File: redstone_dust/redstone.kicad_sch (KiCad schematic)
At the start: 61 parts, among them J1 1x4_Pogo, J2 1x4_Pogo, J3 1x4_Pogo, J4 1x4_Pogo, J5 1x4_Pogo, J6 1x4_Pogo, J7 1x4_Pogo, J8 1x4_Pogo, J9 2.54mm_ProgrammingPin, Q1 BC108, Q2 BC108, Q3 BC108, Q4 BC108, SW1 SW_Push_Open, U1 RP2040, U2 RBT05W24S05, U3 TPS62162DSG, U5 W25Q16JVSS

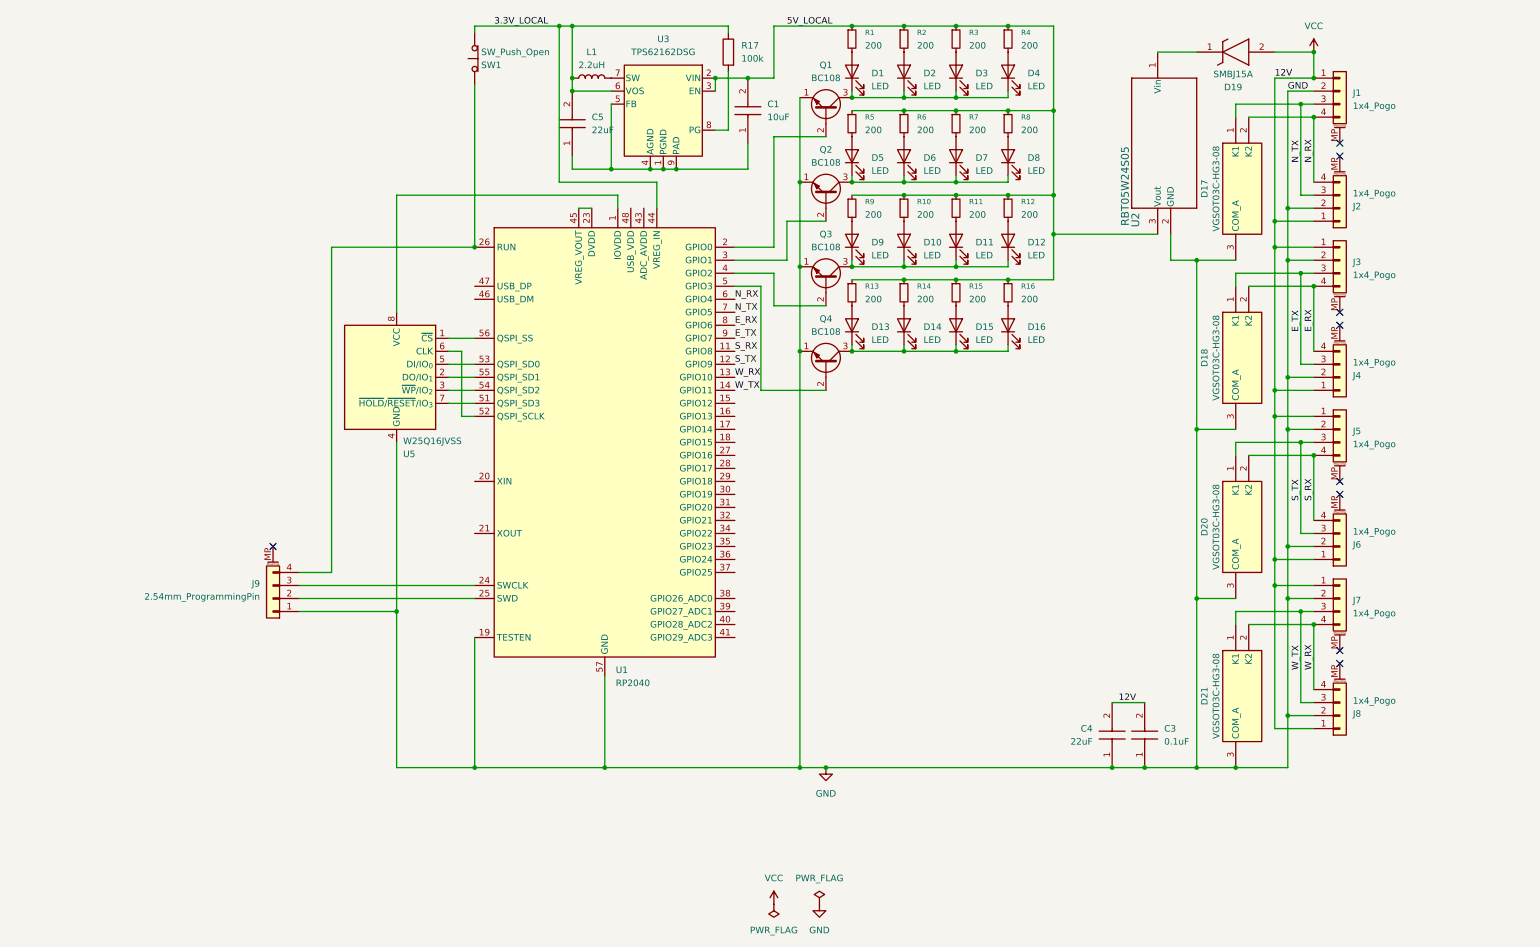
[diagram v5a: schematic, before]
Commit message: add no connect flags to unconnected pins
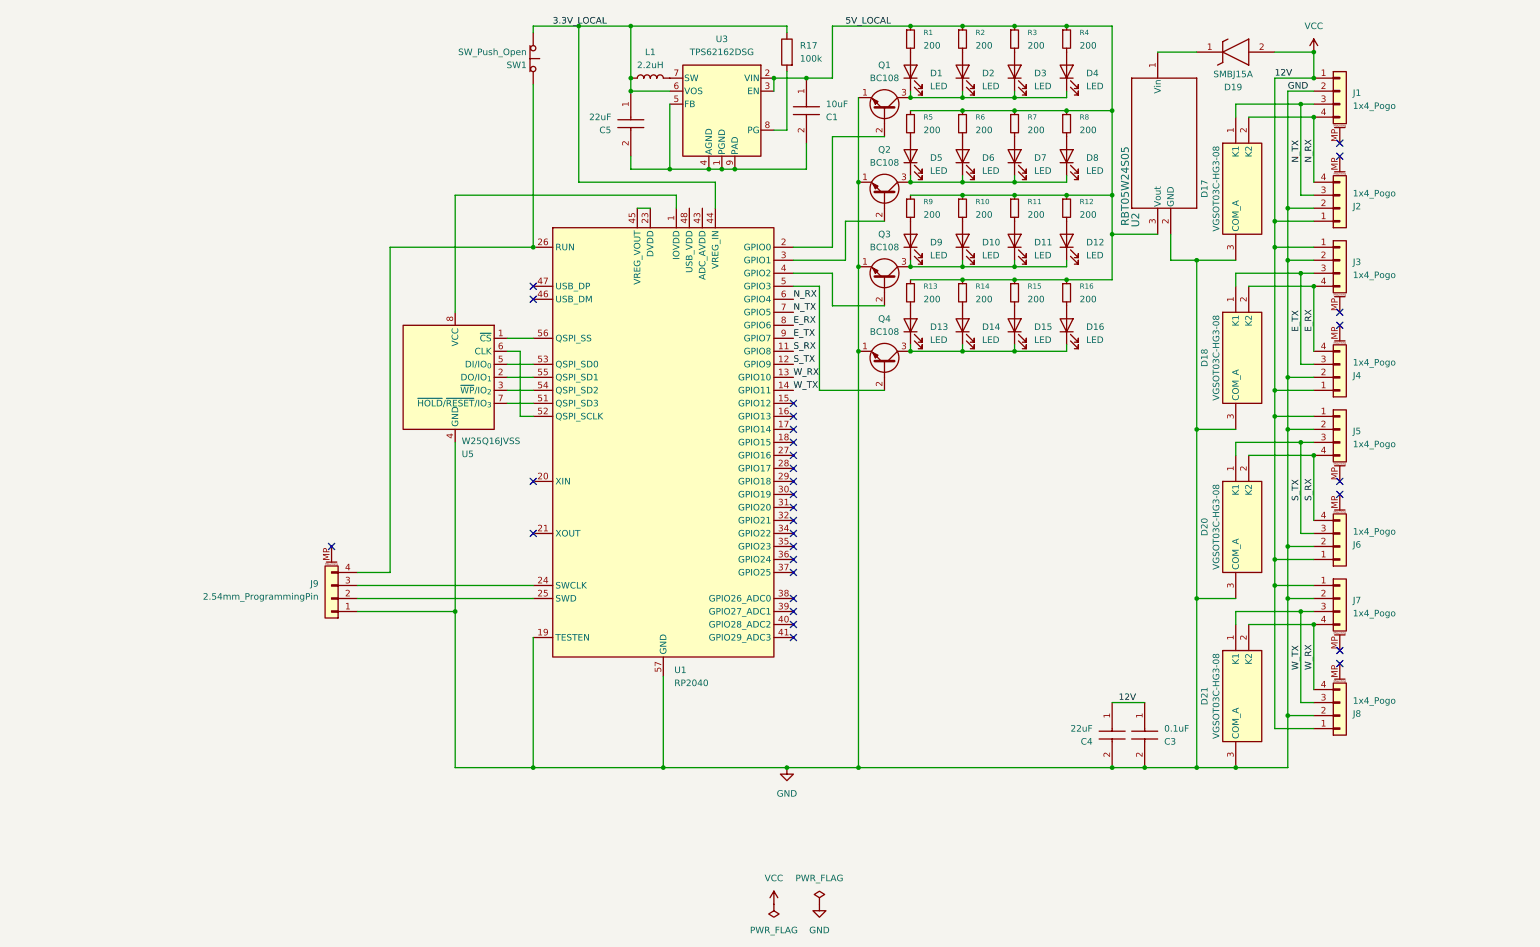
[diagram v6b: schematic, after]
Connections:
- net 3.3V_LOCAL: now also C5.1; no longer C5.2
- net 5V_LOCAL: now also C1.1; no longer C1.2
- net GND: now also C3.2, C4.2; no longer C3.1, C4.1
- net VCC: now also C3.1, C4.1; no longer C3.2, C4.2
- net at U3.1 (PGND), U3.4 (AGND), U3.5 (FB)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: now also C1.2, C5.2; no longer C1.1, C5.1
- no-connect marks 9 -> 31
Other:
- moved on the sheet: C1, C5, D1, D10, D11, D12, D13, D14, D15, D16, D2, D3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

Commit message: run erc and fix some errors
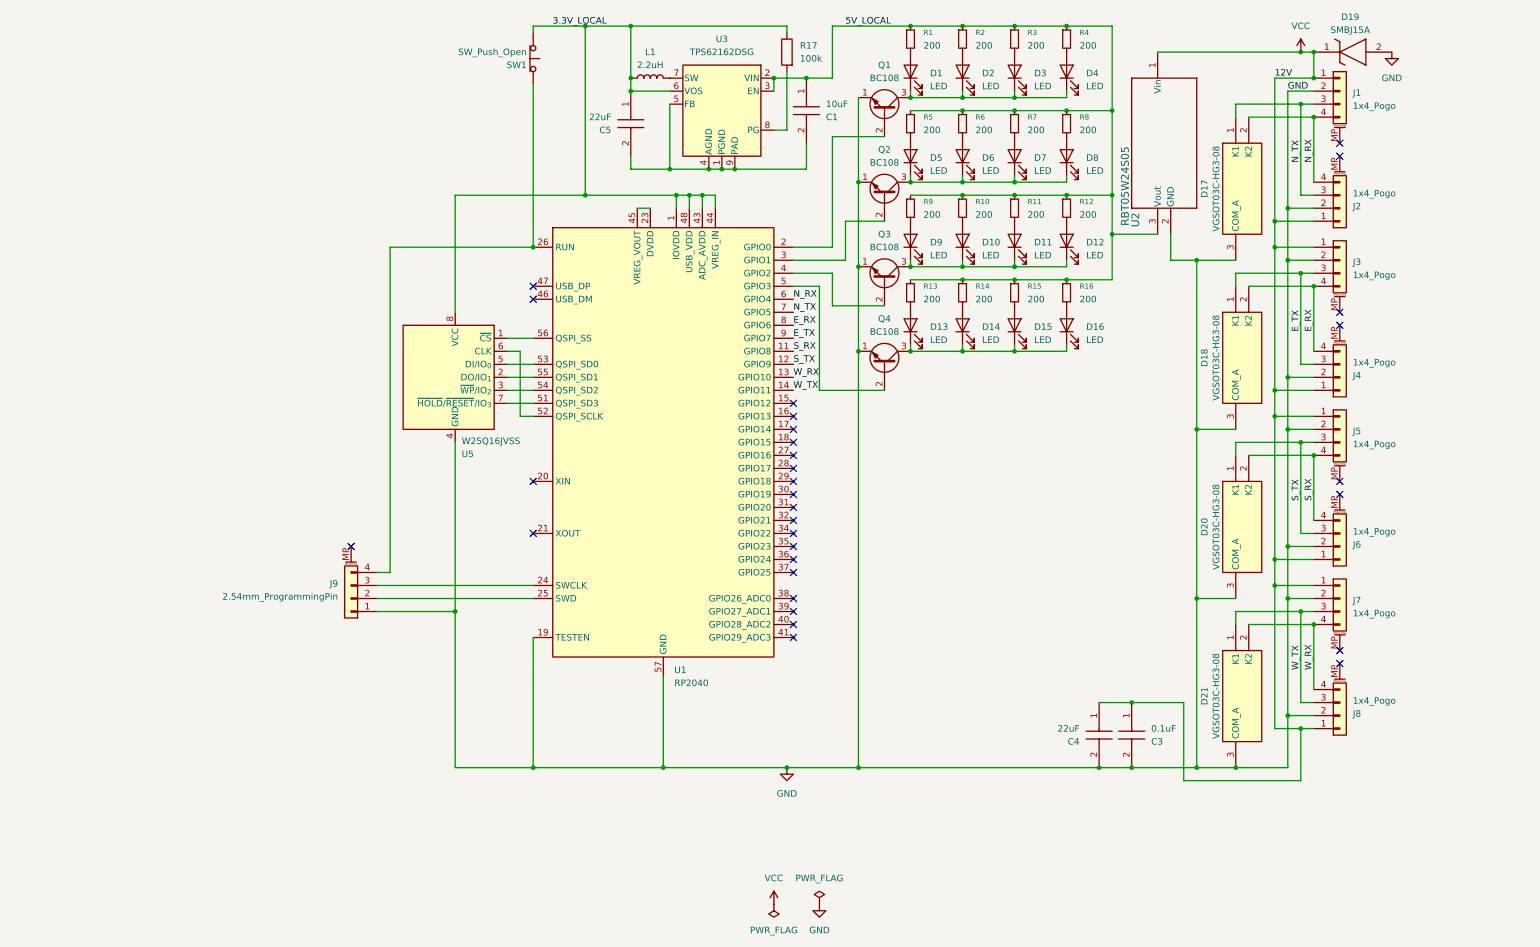
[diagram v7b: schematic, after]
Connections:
- net 3.3V_LOCAL: now also U1.1 (IOVDD), U1.10 (IOVDD), U1.22 (IOVDD), U1.33 (IOVDD), U1.42 (IOVDD), U1.43 (ADC_AVDD), U1.48 (USB_VDD), U1.49 (IOVDD), U5.8 (VCC)
- net GND: now also D19.2 (A)
- net VCC: now also D19.1 (K), U2.1 (Vin); no longer D19.2 (A)
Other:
- moved on the sheet: C3, C4, D19, J9

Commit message: add decoupling capacitors for rp2040
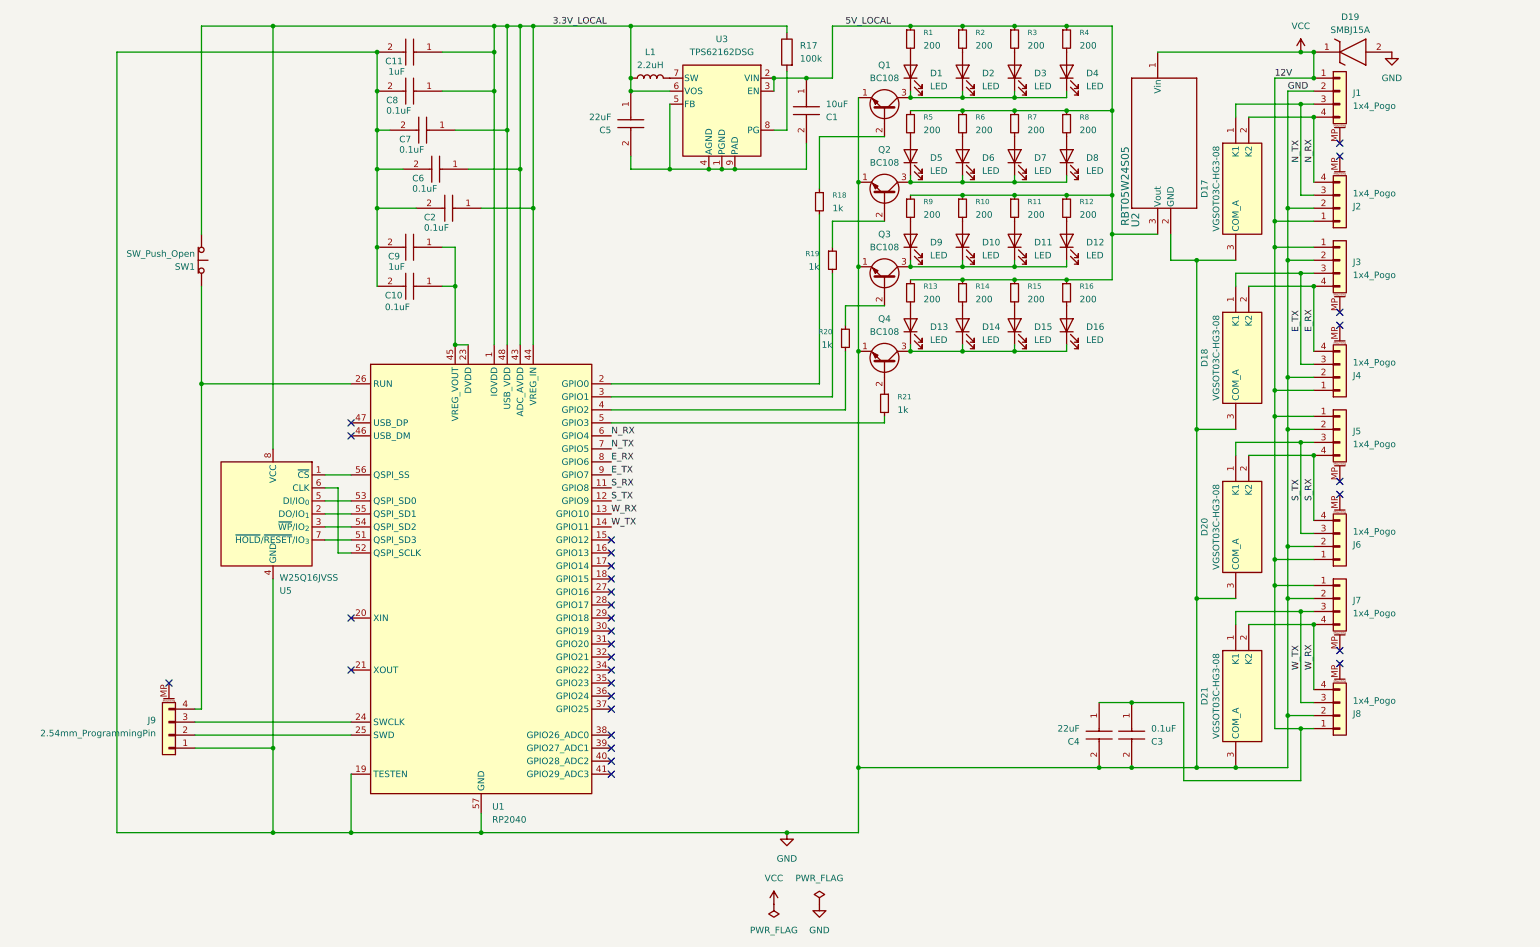
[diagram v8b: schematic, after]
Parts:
- added C10, C2, C6, C7, C8: 0.1uF, CAPC2012X140N, symbol SamacSys_Parts:C0805F104K1RACAUTO
- added C11, C9: 1uF, CAPC0603X33N, symbol SamacSys_Parts:GRM033D70E105ME15D
- added R18, R19, R20, R21: 1k, symbol Device:R_Small
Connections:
- net 3.3V_LOCAL: now also C11.1, C2.1, C6.1, C7.1, C8.1
- net GND: now also C10.2, C11.2, C2.2, C6.2, C7.2, C8.2, C9.2
- net at Q4.2 (B): now also R21.1; no longer U1.5 (GPIO3)
- net at Q2.2 (B): now also R19.1; no longer U1.3 (GPIO1)
- net at Q3.2 (B): now also R20.1; no longer U1.4 (GPIO2)
- net at Q1.2 (B): now also R18.1; no longer U1.2 (GPIO0)
- net at U1.23 (DVDD), U1.45 (VREG_VOUT), U1.50 (DVDD): now also C10.1, C9.1
- new net: R18.2, U1.2 (GPIO0)
- new net: R19.2, U1.3 (GPIO1)
- new net: R20.2, U1.4 (GPIO2)
- new net: R21.2, U1.5 (GPIO3)
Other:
- moved on the sheet: J9, SW1, U1, U5
